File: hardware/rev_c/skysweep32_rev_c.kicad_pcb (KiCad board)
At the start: 4 copper layers, 120 x 85 mm, 67 parts, among them J1 USB4105-GF-A, J2 Molex 104031-0811, J3 OLED STEMMA QT, J4 OPTIONAL VIBRATION MOTOR, J5 SUB-GHZ SMA, Q1 AO3400A, Q2 AO3400A, SW1 RESET, SW2 BOOT, SW3 USER, U1 ESP32-S3-WROOM-1-N8, U2 USBLC6-2SC6, U3 AP63203WU-7

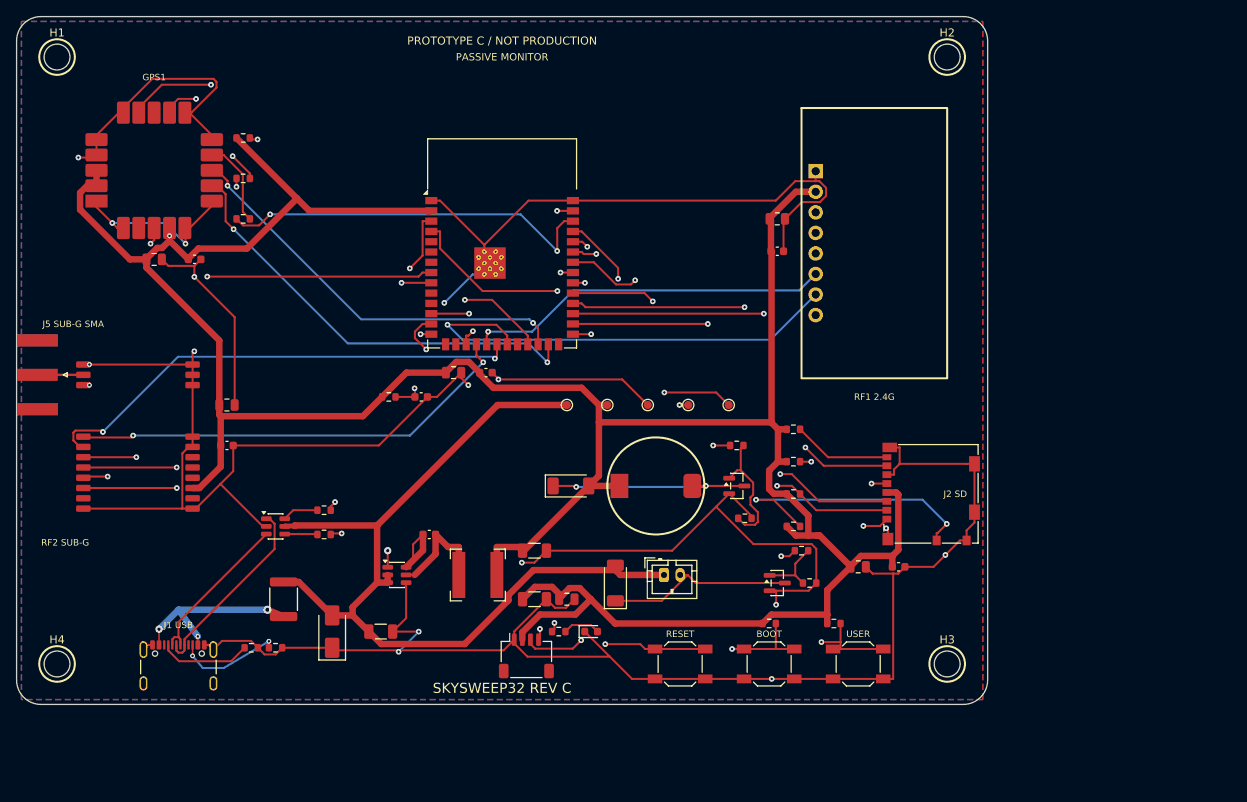
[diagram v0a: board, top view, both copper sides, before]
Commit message: fix(hardware): close Rev C prototype review gaps
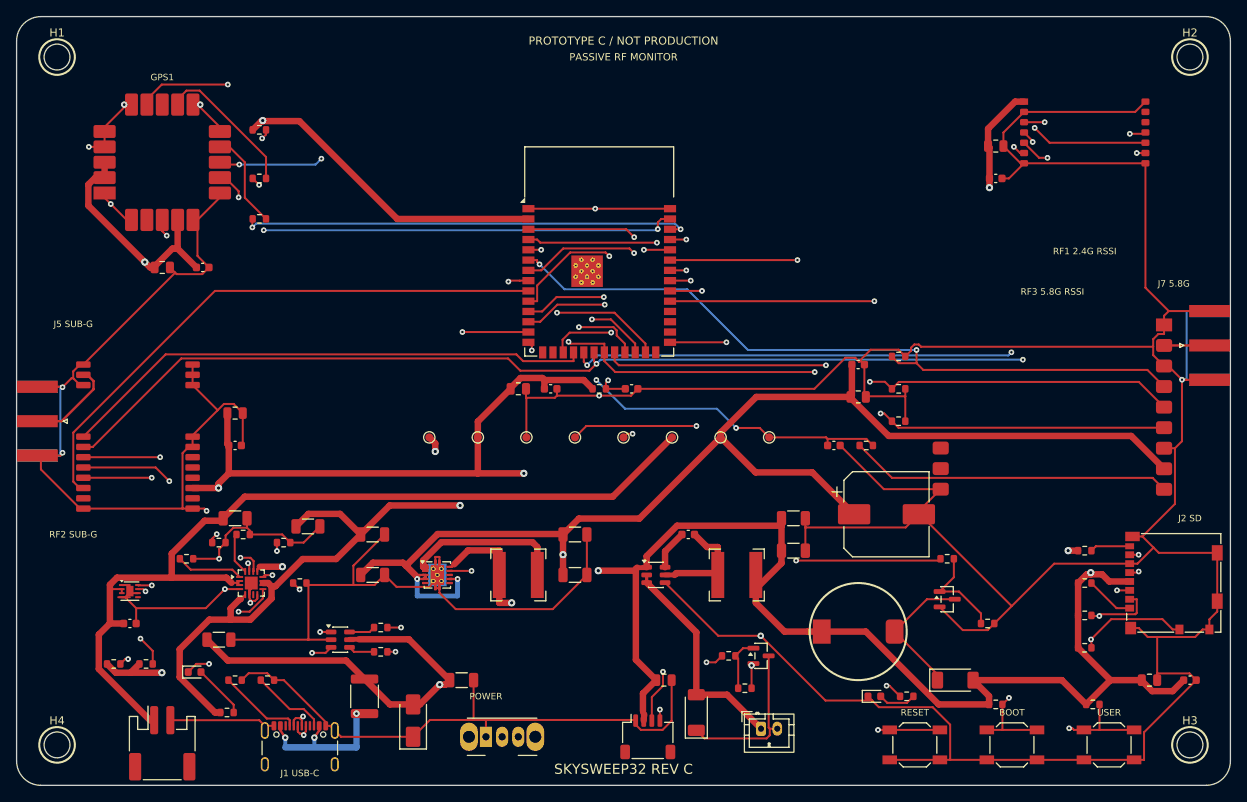
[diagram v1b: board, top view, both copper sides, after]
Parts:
- added C17: 10u, Capacitor_SMD:C_1206_3216Metric, F.Cu at (25.0, 77.0)
- added C18: 10u, Capacitor_SMD:C_1206_3216Metric, F.Cu at (27.0, 62.0)
- added C19: 10u, Capacitor_SMD:C_1206_3216Metric, F.Cu at (36.0, 63.0)
- added C20: 22u, Capacitor_SMD:C_1206_3216Metric, F.Cu at (44.0, 64.0)
- added C21: 22u, Capacitor_SMD:C_1206_3216Metric, F.Cu at (44.0, 69.0)
- added C22: 22u, Capacitor_SMD:C_1206_3216Metric, F.Cu at (69.0, 64.0)
- added C23: 22u, Capacitor_SMD:C_1206_3216Metric, F.Cu at (69.0, 69.0)
- added C24: 100n, Capacitor_SMD:C_0603_1608Metric, F.Cu at (104.0, 43.0)
- added C25: 10u, Capacitor_SMD:C_0805_2012Metric, F.Cu at (104.0, 47.0)
- added C26: 470u 10V, Capacitor_SMD:CP_Elec_10x10, F.Cu at (107.5, 61.5)
- added C29: 100n, Capacitor_SMD:C_0603_1608Metric, F.Cu at (14.0, 75.0)
- added C30: 10n, Capacitor_SMD:C_0603_1608Metric, F.Cu at (101.0, 53.0)
- added D5: CHARGE, LED_SMD:LED_0603_1608Metric, F.Cu at (22.0, 81.0)
- added J6: BATTERY — ADAFRUIT PID 328, Connector_JST:JST_PH_S2B-PH-SM4-TB_1x02-1MP_P2.00mm_Horizontal, F.Cu at (18.0, 89.8)
- added J7: 5.8-GHZ SMA, Connector_Coaxial:SMA_Amphenol_132289_EdgeMount, F.Cu at (147.4, 40.6)
- added L2: 1uH SRN6028C-1R0Y, Inductor_SMD:L_Bourns-SRN6028, F.Cu at (62.0, 69.0)
- added R20: 10k, Resistor_SMD:R_0603_1608Metric, F.Cu at (21.0, 67.0)
- added R21: 46.4k, Resistor_SMD:R_0603_1608Metric, F.Cu at (25.0, 65.0)
- added R22: 1.13k, Resistor_SMD:R_0603_1608Metric, F.Cu at (28.0, 64.0)
- added R23: 1.18k, Resistor_SMD:R_0603_1608Metric, F.Cu at (33.0, 65.0)
- added R24: 4.12k, Resistor_SMD:R_0603_1608Metric, F.Cu at (35.0, 70.0)
- added R25: 1.5k, Resistor_SMD:R_0603_1608Metric, F.Cu at (26.0, 86.0)
- added R26: 4.7k, Resistor_SMD:R_0603_1608Metric, F.Cu at (12.0, 80.0)
- added R27: 4.7k, Resistor_SMD:R_0603_1608Metric, F.Cu at (16.0, 80.0)
- added R28: 100k, Resistor_SMD:R_0603_1608Metric, F.Cu at (109.0, 42.0)
- added R29: 100k, Resistor_SMD:R_0603_1608Metric, F.Cu at (109.0, 46.0)
- added R30: 100k, Resistor_SMD:R_0603_1608Metric, F.Cu at (109.0, 50.0)
- added R31: 1k, Resistor_SMD:R_0603_1608Metric, F.Cu at (105.0, 53.0)
- added RF3: RX5808-2012-12P, SkySweep32RevC:Module_RX5808_2012_12P, F.Cu at (128.0, 48.0)
- added SW4: SYSTEM POWER, Button_Switch_THT:SW_Slide_SPDT_Angled_CK_OS102011MA1Q, F.Cu at (58.0, 89.0)
- added TP6: BAT_CELL, TestPoint:TestPoint_Pad_D1.0mm, F.Cu at (81.0, 52.0)
- added TP7: SYS_5V, TestPoint:TestPoint_Pad_D1.0mm, F.Cu at (87.0, 52.0)
- added TP8: RX5808_RSSI_ADC, TestPoint:TestPoint_Pad_D1.0mm, F.Cu at (93.0, 52.0)
- added U4: BQ24074RGTR, Package_DFN_QFN:VQFN-16-1EP_3x3mm_P0.5mm_EP1.6x1.6mm, F.Cu at (29.0, 70.0)
- added U5: TPS61232DRCR, Package_SON:Texas_S-PVSON-N10_ThermalVias, F.Cu at (52.0, 69.0)
- added U6: MAX17048G+T10, Package_DFN_QFN:DFN-8-1EP_2x2mm_P0.5mm_EP0.9x1.3mm, F.Cu at (14.0, 71.0)
- RF1: value E01-ML01DP5 -> E28-2G4M12SX; footprint SkySweep32RevC:Module_Ebyte_E01_ML01DP5 -> SkySweep32RevC:Module_Ebyte_E28_2G4M12SX
- U1: value ESP32-S3-WROOM-1-N8 -> ESP32-S3-WROOM-1-N16R8
- moved D2 53.2 mm to (116.0, 82.0)
- moved R17 43.7 mm to (110.0, 84.0)
- moved R11 39.0 mm to (132.0, 66.0)
- moved R12 39.0 mm to (132.0, 70.0)
- moved R13 39.0 mm to (132.0, 74.0)
- moved R14 39.0 mm to (132.0, 78.0)
- moved C14 38.6 mm to (140.0, 82.0)
- moved C15 38.6 mm to (145.0, 82.0)
- moved D3 35.9 mm to (106.0, 84.0)
- moved R7 33.5 mm to (133.0, 85.0)
- moved R16 32.7 mm to (120.0, 75.0)
- moved SW3 32.6 mm to (135.0, 90.0)
- moved C4 32.6 mm to (96.0, 66.0)
- moved C3 32.2 mm to (96.0, 62.0)
- moved C2 32.0 mm to (83.0, 64.0)
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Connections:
- D4 pad 2: VBUS_PROTECTED -> SYS_5V
- J2 pad 3: SD_SPI_MOSI -> RF_SPI_MOSI
- J2 pad 5: SD_SPI_SCK -> RF_SPI_SCK
- J2 pad 7: SD_SPI_MISO -> RF_SPI_MISO
- J4 pad 1: VBUS_PROTECTED -> SYS_5V
- RF1 pad 1: GND -> 3V3
- RF1 pad 2: 3V3 -> GND
- RF1 pad 3: NRF24_CE -> RF_SPI_MISO
- RF1 pad 4: NRF24_CSN -> RF_SPI_MOSI
- RF1 pad 6: RF_SPI_MOSI -> SX1281_CSN
- RF1 pad 7: RF_SPI_MISO -> GND
- RF1 pad 8: unconnected-(RF1-Pin_8-Pad8) -> GND
- U1 pad 10: unconnected-(U1-IO17-Pad10) -> SX1281_RESET
- U1 pad 11: unconnected-(U1-IO18-Pad11) -> SX1281_DIO1
- U1 pad 12: NRF24_CE -> SX1281_BUSY
- U1 pad 17: NRF24_CSN -> SX1281_CSN
- U1 pad 22: unconnected-(U1-IO14-Pad22) -> RX5808_CH3
- U1 pad 28: SD_SPI_MOSI -> unconnected-(U1-IO35-Pad28)
- U1 pad 29: SD_SPI_SCK -> unconnected-(U1-IO36-Pad29)
- U1 pad 30: SD_SPI_MISO -> unconnected-(U1-IO37-Pad30)
- U1 pad 5: unconnected-(U1-IO5-Pad5) -> RX5808_RSSI_ADC
- U1 pad 6: unconnected-(U1-IO6-Pad6) -> RX5808_CH1
- U1 pad 7: unconnected-(U1-IO7-Pad7) -> RX5808_CH2
- U3 pad 2: VBUS_PROTECTED -> SYS_5V
- U3 pad 3: VBUS_PROTECTED -> SYS_5V
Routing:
- net GND: track 619.5 -> 915.0 mm, vias 17 -> 15
- net SYS_5V: track 0.00 -> 223.4 mm, vias 0 -> 3
- net 3V3: track 353.9 -> 490.2 mm, vias 2 -> 9
- net VSYS_BAT: track 0.00 -> 115.1 mm, vias 0 -> 2
- net BAT_CELL: track 0.00 -> 112.6 mm
- net RX5808_CH2: track 0.00 -> 103.8 mm, vias 0 -> 2
- net SX1281_DIO1: track 0.00 -> 91.0 mm, vias 0 -> 2
- net SX1281_BUSY: track 0.00 -> 90.3 mm, vias 0 -> 2
- net SX1281_RESET: track 0.00 -> 89.6 mm, vias 0 -> 2
- net RX5808_CH1: track 0.00 -> 89.5 mm, vias 0 -> 2
- net RF_SPI_MISO: track 118.2 -> 207.5 mm, vias 2 -> 5
- net RF_SPI_MOSI: track 111.8 -> 197.0 mm, vias 2 -> 5
- net I2C_SCL: track 96.5 -> 179.3 mm, vias 3 -> 5
- net RF_SPI_SCK: track 110.7 -> 186.5 mm, vias 2 -> 4
- net SX1281_CSN: track 0.00 -> 73.9 mm, vias 0 -> 2
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- removed copper zone on B.Cu, net GND
- removed copper zone on F.Cu, net GND
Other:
- board size 120 x 85 mm -> 150 x 95 mm
- board text added: "J1 USB-C"
- board text added: "J5 SUB-G"
- board text added: "J7 5.8G"
- board text added: "PASSIVE RF MONITOR"
- board text added: "POWER"
- board text added: "RF1 2.4G RSSI"
- board text added: "RF3 5.8G RSSI"
- board text removed: "J1 USB"
- board text removed: "J5 SUB-G SMA"
- board text removed: "PASSIVE MONITOR"
- board text removed: "RF1 2.4G"

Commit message: fix(hardware): correct Rev C electrical integration
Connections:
- D1 pad 1: GND -> VBUS_PROTECTED
- D1 pad 2: VBUS_PROTECTED -> GND
- D2 pad 1: BUZZER_DRAIN -> 3V3
- D2 pad 2: 3V3 -> BUZZER_DRAIN
- D4 pad 1: VIBRATION_DRAIN -> SYS_5V
- D4 pad 2: SYS_5V -> VIBRATION_DRAIN
- U6 pad 6: GND -> unconnected-(U6-Pin_6-Pad6)
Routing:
- net SYS_5V: track 223.4 -> 253.2 mm, vias 3 -> 6
- net VIBRATION_DRAIN: track 20.4 -> 43.9 mm, vias 0 -> 2
- net GND: track 915.0 -> 903.6 mm, vias 15 -> 18
- net VBUS_PROTECTED: track 109.8 -> 120.0 mm, vias 3 -> 6
- net 3V3: track 490.2 -> 499.5 mm, vias 9 -> 11
- net BUZZER_DRAIN: track 17.3 -> 22.9 mm, vias 0 -> 2
